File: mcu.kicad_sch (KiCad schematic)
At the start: 34 parts, among them J2 USB-C, J3 UART0, J4 I2C / Qwiic, J5 SPI, J6 WS2812, J7 Spare IO, J8 Rail break-out, SW1 RESET, SW2 BOOT, U4 ESP32-S3-WROOM-1-N16R8, U5 USBLC6-2SC6, U6 74AHCT1G125

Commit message: Power-fail ride-through: detect, coast, shed; board grows to 84 x 100
The ignition cuts this board's power with a log file open, every drive.
Three new pieces make that survivable, all simulated before layout:

- Detect: TLV431 + 100k/12.7k divider on VBAT_F, AHEAD of the ideal
  diode, asserting PWR_FAIL (IO15) at 11.0 V with ~0.3 V hysteresis.
  The harness collapses microseconds after the key turns while +VBAT
  coasts, so the warning costs no stored energy.
- Coast: two 220 uF/100 V cans join the 100 uF on +VBAT. 540 uF on the
  input rail, where a volt of headroom is worth most.
- Shed: AO3401 + 2N7002 high-side switch on the sensor rail (SENS_EN,
  IO16, off at reset), with PF1 moved behind it so a tripped sensor
  fuse can also be power-cycled from firmware.

Simulated end to end: detection <1 ms after the cut, then 108 ms to
converter dropout with sensors shed, 53 ms without -- the switch doubles
the flush budget. ISO pulse 1's brownout shortens from 8.2 to 5.6 ms.

The two cans plus the detector had no free board left on 84 x 84, so the
board grows to 84 x 100 (still JLC's cheap tier): bottom-edge furniture
and mounting holes move down 16 mm, one can per side, and the detector/
switch column gets its own placement zone. Also included from the audit:
the 3V3 buck's own input capacitor pair at its VIN pin (it was reaching
12.6 mm across to the 5 V island's), the CAN transceiver and AHCT buffer
bypasses pinned at their pins, and Power-class tracks at 0.55 mm to clear
IPC-2221 for 2 A at a 20 C rise.

Hard-won generator fix: a literal newline inside a symbol property is
accepted by KiCad's loader but silently breaks connectivity for every
symbol after it in the file -- the netlist dropped 45 components with no
error pointing anywhere near the cause. The emitter now flattens all
whitespace in property strings.

Board: 0 DRC violations, 0 unconnected, physical audit clean end to end.
185 components, 111 nets, ERC clean, netlist verified node-for-node.

Co-Authore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
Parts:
- removed C21: 1uF, Capacitor_SMD:C_0805_2012Metric, symbol Device:C
- removed C22, C25: 10uF, Capacitor_SMD:C_1206_3216Metric, symbol Device:C
- removed C23, C24: 100nF, Capacitor_SMD:C_0805_2012Metric, symbol Device:C
- removed R16, R17, R22: 10k, Resistor_SMD:R_0805_2012Metric, symbol Device:R
- removed R18, R19: 5.1k, Resistor_SMD:R_0805_2012Metric, symbol Device:R
- removed R20, R21: 4.7k, Resistor_SMD:R_0805_2012Metric, symbol Device:R
- removed U4: ESP32-S3-WROOM-1-N16R8, RF_Module:ESP32-S3-WROOM-1, symbol RF_Module:ESP32-S3-WROOM-1
- added C28, C29, C31, C32: 100nF, Capacitor_SMD:C_0805_2012Metric, symbol Device:C
- added C30: 10uF, Capacitor_SMD:C_1206_3216Metric, symbol Device:C
- added R28: 4.7k, Resistor_SMD:R_0805_2012Metric, symbol Device:R
- added R29, R32, R33, R34: 10k, Resistor_SMD:R_0805_2012Metric, symbol Device:R
- added R30: 33, Resistor_SMD:R_0805_2012Metric, symbol Device:R
- added R31: 100, Resistor_SMD:R_0805_2012Metric, symbol Device:R
- added U7: 74AHCT1G125, Package_TO_SOT_SMD:SOT-23-5, symbol 74xGxx:74AHCT1G125
- C26: value 100nF -> 1uF; Note USBLC6-2SC6 VBUS pin decoupling; the ST datasheet asks for 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 -> EN reset delay
- C27: value 100nF -> 10uF; footprint Capacitor_SMD:C_0805_2012Metric -> Capacitor_SMD:C_1206_3216Metric; Note AHCT decoupling -> (none)
- J7: Note IO3/IO45/IO46 are strapping pins, each with a 10k pull-down -- anything attached must not fight them at boot. IO15/IO16 are ordinary GPIOs, free since the status LEDs came off. The ground pin is here so a probe or a ribbon has a return -> IO3/IO45/IO46 are strapping pins, each with a 10k pull-down -- anything attached must not fight them at boot. Pins 4 and 5 are no longer spare: IO15 is the power-fail interrupt and IO16 is the sensor-rail enable. They stay on the header as probe points, so the ride-through can be watched on a scope without unsoldering anything, but nothing else may drive them. The ground pin is here so a probe or a ribbon has a return
- R23: value 33 -> 10k; Note Edge-rate limit into the level shifter -> (none)
- R24: value 100 -> 10k; Note Series termination into the strip. The buffer drove the con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 -> (none)
- R25: value 10k -> 5.1k; Note Strapping pin held low at boot -> (none)
- R26: value 10k -> 5.1k; Note Strapping pin: VDD_SPI = 3.3V -> (none)
- R27: value 10k -> 4.7k; Note Strapping pin: normal boot mode -> (none)
- U5: value USBLC6-2SC6 -> ESP32-S3-WROOM-1-N16R8; footprint Package_TO_SOT_SMD:SOT-23-6 -> RF_Module:ESP32-S3-WROOM-1; symbol Power_Protection:USBLC6-2SC6 -> RF_Module:ESP32-S3-WROOM-1; MPN USBLC6-2SC6 -> ESP32-S3-WROOM-1-N16R8; Note USB ESD clamp -> 16MB flash / 8MB octal PSRAM. Pins 28-30 (IO35/36/37) are c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
- U6: value 74AHCT1G125 -> USBLC6-2SC6; footprint Package_TO_SOT_SMD:SOT-23-5 -> Package_TO_SOT_SMD:SOT-23-6; symbol 74xGxx:74AHCT1G125 -> Power_Protection:USBLC6-2SC6; MPN SN74AHCT1G125DBVR -> USBLC6-2SC6; Note 5 V buffer so WS2812 DIN is a real 5 V rail, not 3.3 V hopi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 -> USB ESD clamp
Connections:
- net +3V3: now also C27.1, R23.1, R24.1, R27.1, U5.2 (3V3), C28.1, C29.1, R28.1, R29.2
- net +5V: now also C32.1, U7.5 (VCC); no longer C27.1, U6.5 (VCC)
- net AIN1: now also U5.39 (IO1)
- net AIN2: now also U5.38 (IO2)
- net AIN3: now also U5.4 (IO4)
- net AIN4: now also U5.5 (IO5)
- net CAN_RX: now also U5.11 (IO18)
- net CAN_S: now also U5.23 (IO21)
- net CAN_TX: now also U5.10 (IO17)
- net GND: now also U5.1 (GND), U5.40 (GND), U5.41 (GND), U6.2 (GND), C28.2, C29.2, C30.2, C31.2, C32.2, R32.2, R33.2, R34.2, U7.1, U7.3 (GND); no longer R27.2, U5.2 (GND), U6.1, U6.3 (GND)
- net I2C_SCL: now also U5.32 (IO39), R28.2
- net I2C_SDA: now also R27.2, U5.31 (IO38)
- net IO3: now also U5.15 (IO3), R32.1; no longer R25.1
- net IO45: now also U5.26 (IO45), R33.1; no longer R26.1
- net IO46: now also U5.16 (IO46), R34.1; no longer R27.1
- net LED_DIN: now also R31.1, U7.4; no longer R24.1, U6.4
- net LED_DIN_A: now also R30.2, U7.2; no longer R23.2, U6.2
- net LED_DIN_J: now also R31.2; no longer R24.2
- net LED_DIN_MCU: now also U5.25 (IO48), R30.1; no longer R23.1
- net MCU_BOOT: now also R24.2, U5.27 (IO0)
- net MCU_EN: now also C26.1, R23.2, U5.3 (EN)
- net SD_CD: now also U5.12 (IO8)
- net SD_CLK: now also U5.22 (IO14)
- net SD_CMD: now also U5.21 (IO13)
- net SD_D0: now also U5.20 (IO12)
- net SD_D1: now also U5.19 (IO11)
- net SD_D2: now also U5.18 (IO10)
- net SD_D3: now also U5.17 (IO9)
- net SD_PWR_EN: now also U5.7 (IO7)
- net SPI_CS: now also U5.24 (IO47), R29.1
- net SPI_MISO: now also U5.34 (IO41)
- net SPI_MOSI: now also U5.35 (IO42)
- net SPI_SCK: now also U5.33 (IO40)
- net UART_RX: now also U5.36 (RXD0)
- net UART_TX: now also U5.37 (TXD0)
- net USB_CC1: now also R25.1
- net USB_CC2: now also R26.1
- net USB_DM: now also U5.13 (USB_D-), U6.4 (I/O2); no longer U5.4 (I/O2)
- net USB_DM_CON: now also U6.3 (I/O2); no longer U5.3 (I/O2)
- net USB_DP: now also U5.14 (USB_D+), U6.6 (I/O1); no longer U5.6 (I/O1)
- net USB_DP_CON: now also U6.1 (I/O1); no longer U5.1 (I/O1)
- net VBAT_SNS: now also U5.6 (IO6)
- net VBUS: now also U6.5 (VBUS), C30.1, C31.1; no longer C26.1, U5.5 (VBUS)
- net IO15 renamed PWR_FAIL
- net PWR_FAIL: now also U5.8 (IO15)
- net IO16 renamed SENS_EN
- net SENS_EN: now also U5.9 (IO16)
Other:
- moved on the sheet: C26, C27, R23, R24, R25, R26, R27

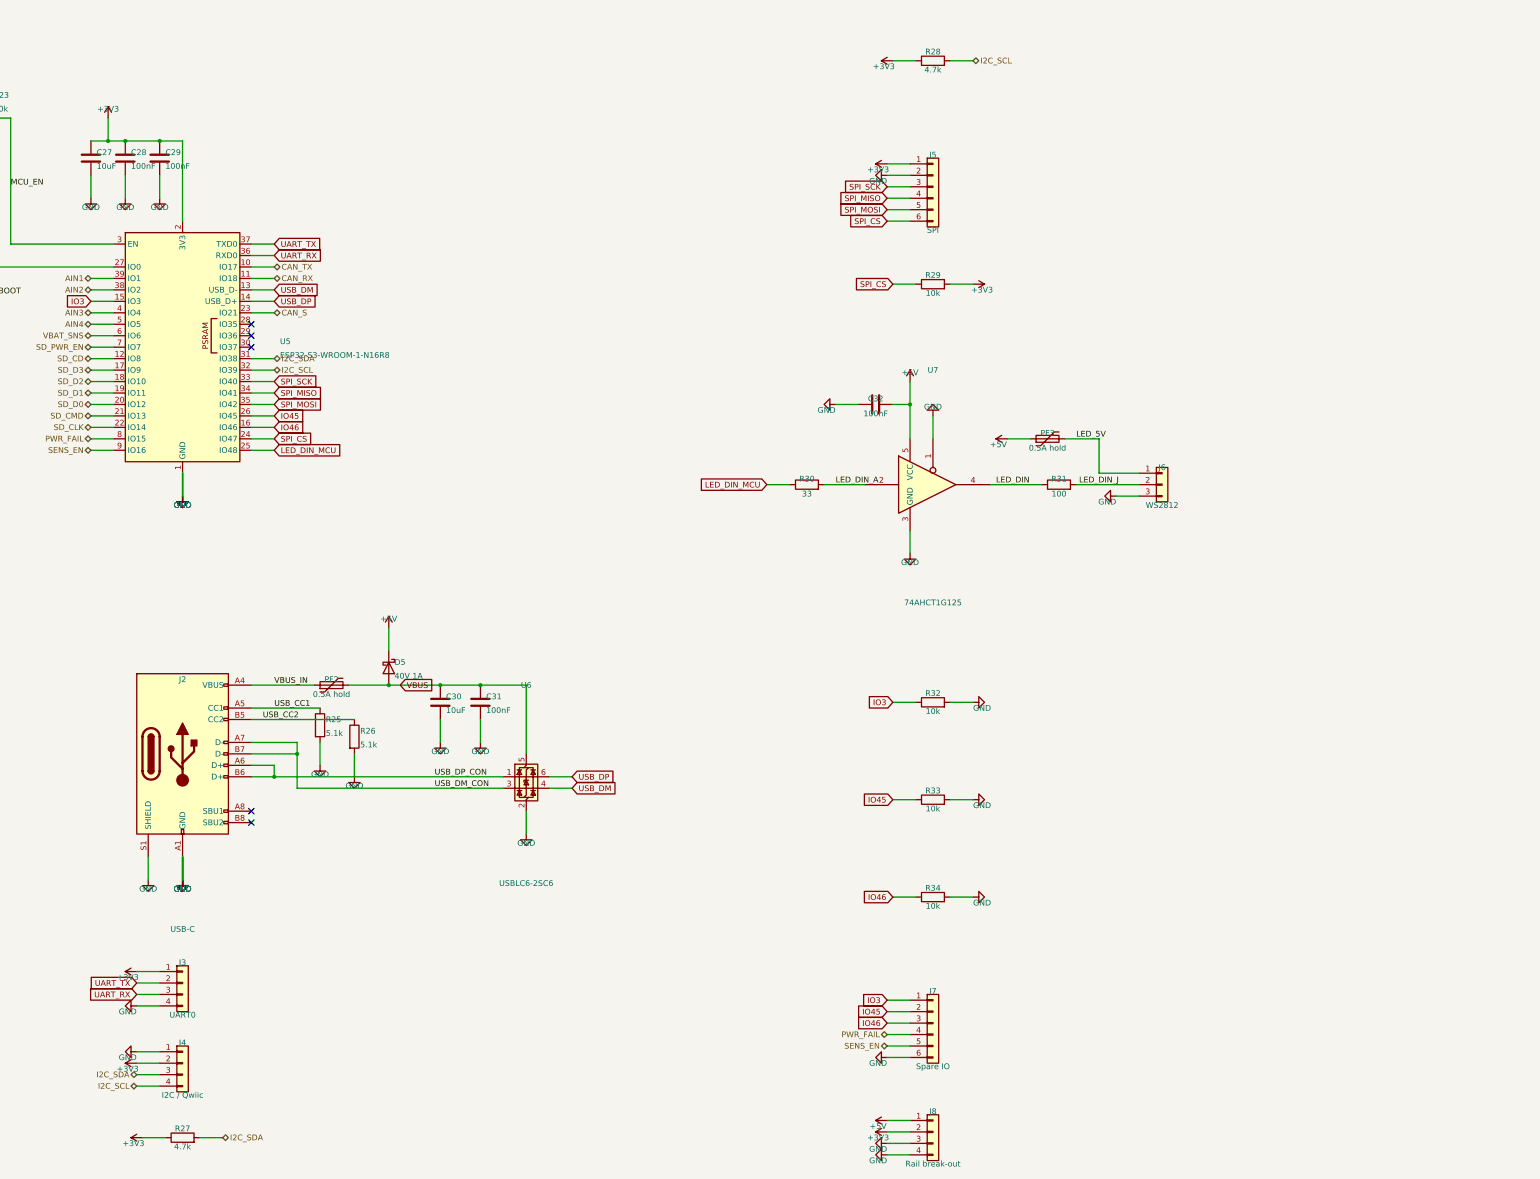
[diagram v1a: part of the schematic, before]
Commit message: USB OVP, card-slot ESD, SD test points, and a gold-standard schematic
Hardware, all simulation- or review-driven:
- USB overvoltage cutoff: TLV431 + AO3401 + MMBT3906 series switch on
  VBUS, tripping at 5.77 V. Re-simulated: a compliant 5 V source passes
  at 4.99 V, the switch opens at 5.95 V of brick, and the +5V rail never
  exceeds 5.2 V from anything up to 14 V -- where a 9 V brick previously
  drove it to 8.4 V against the TJA1051's 6 V absolute maximum.
  Off-the-shelf OVP parts were rejected first: the TPS25200 class cuts
  off near 7 V, which is no protection for a 6 V limit.
- Two SRV05-4 arrays clamp every microSD card contact (LCSC C13612);
  until now the ESP32's ~2 kV pin diodes were all that stood behind a
  card swapped by hand after every session.
- A second USBLC6 clamps the USB-C CC pins -- the first contacts every
  plug insertion touches, previously landing on bare 5.1k resistors.
- Test points on SD_CLK and SD_CMD, the most likely scope targets at
  bring-up and otherwise reachable only on fine-pitch pads.

The schematic itself was rebuilt to read like a reference design
(RejsaCAN was the benchmark): every circuit is now a hand-drawn block --
power-fail detector, sensor-rail switch, USB OVP, connector pull-
resistor clusters, and a single utility panel for test points, ERC
flags, mounting holes and the power LED. Sentence-length values became
part numbers ("0.2A PTC", "AO3401A", "600R") with ratings kept in
hidden fields, which also answers the external review's value-hygiene
findings. Title blocks carry rev B and a date. The Power sheet shrank
from A2 back to A3 in the process.

gen/README.md now documents the whole pipeline -- stages, the block-
drawing conventions with per-rotation pin geometry, the junction rules,
and the traps (property newlines, off-grid points, anchors keeping
their natural rotation) -- so the next board reuses all of it.

Board: 84 x 100, 0 DRC violations, 0 unconnected, 0 courtyard overlaps,
physical audit clean. BOM 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
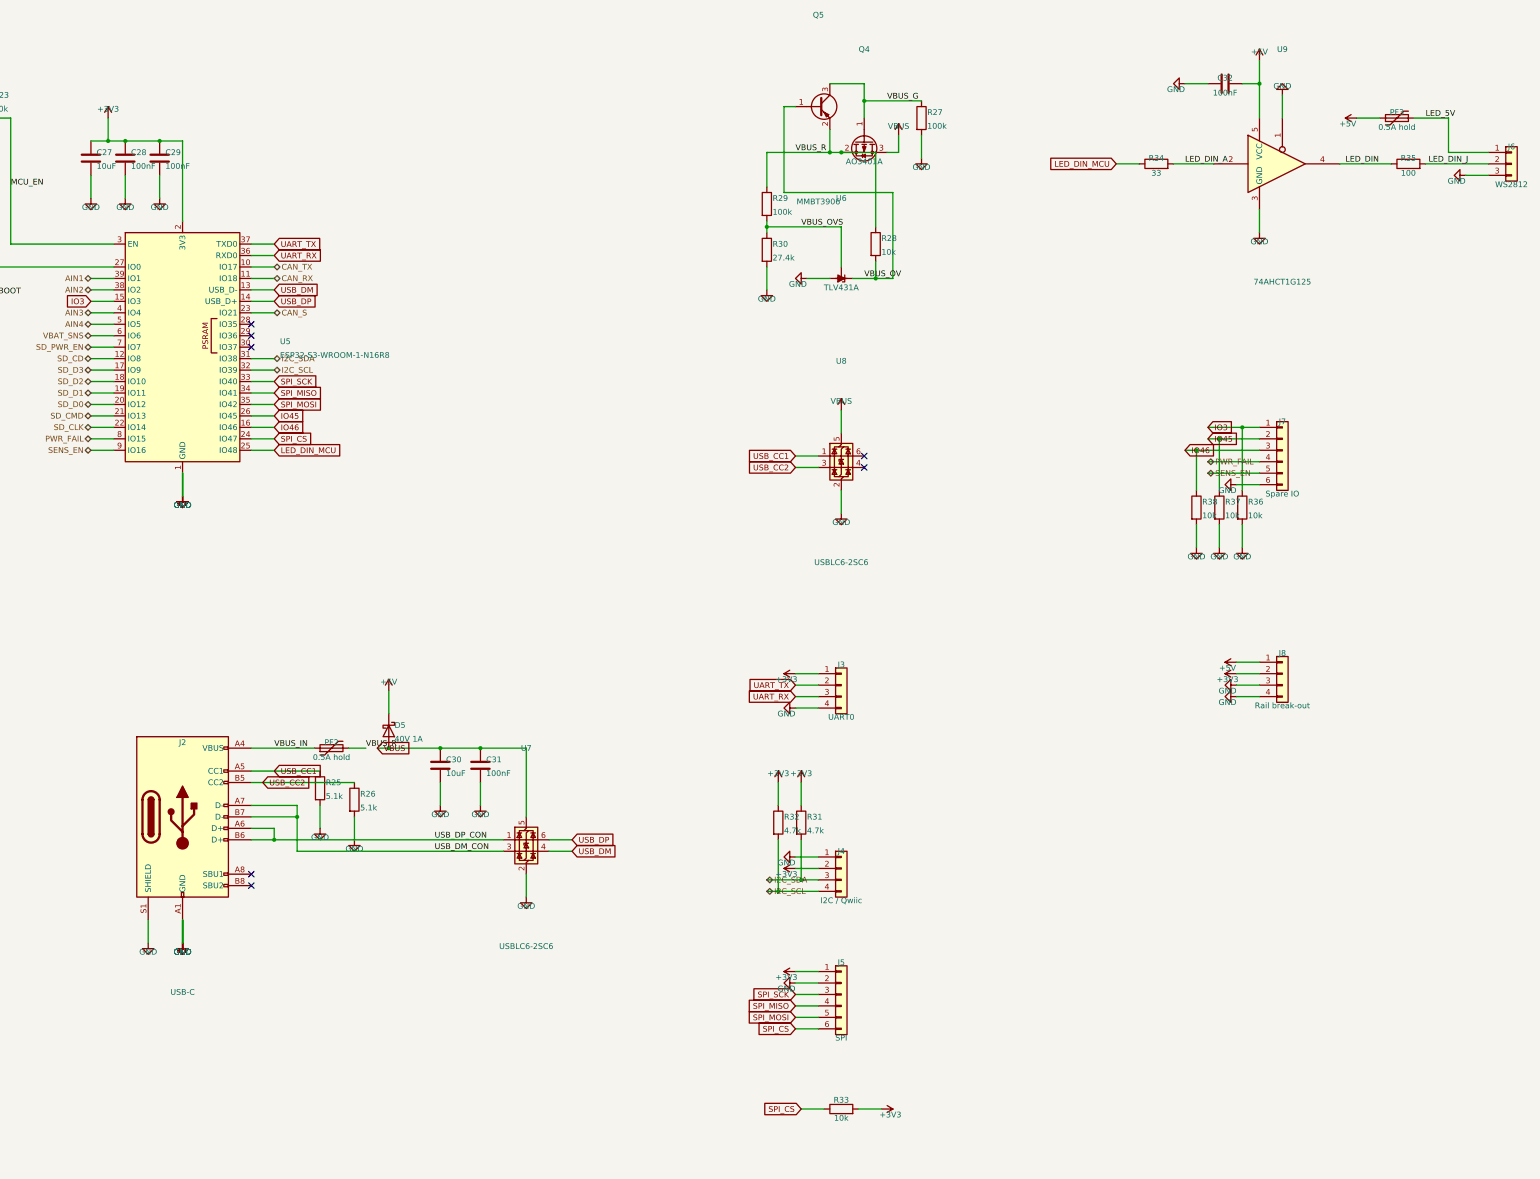
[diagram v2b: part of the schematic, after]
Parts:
- added Q4: AO3401A, Package_TO_SOT_SMD:SOT-23, symbol Transistor_FET:Q_PMOS_GSD
- added Q5: MMBT3906, Package_TO_SOT_SMD:SOT-23, symbol Transistor_BJT:Q_PNP_BEC
- added R35: 100, Resistor_SMD:R_0805_2012Metric, symbol Device:R
- added R36, R37, R38: 10k, Resistor_SMD:R_0805_2012Metric, symbol Device:R
- added U8: USBLC6-2SC6, Package_TO_SOT_SMD:SOT-23-6, symbol Power_Protection:USBLC6-2SC6
- added U9: 74AHCT1G125, Package_TO_SOT_SMD:SOT-23-5, symbol 74xGxx:74AHCT1G125
- R27: value 4.7k -> 100k; Note (none) -> Switch on by default
- R28: value 4.7k -> 10k; Note (none) -> Holds the PNP off while the TLV431 is not conducting
- R29: value 10k -> 100k; Note Holds an attached slave deselected until firmware drives IO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 -> OVP divider upper leg; Tolerance (none) -> 1%
- R30: value 33 -> 27.4k; Note Edge-rate limit into the level shifter -> Trip at 1.24V x 127.4/27.4 = 5.77V: above a compliant sourc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; Tolerance (none) -> 1%
- R31: value 100 -> 4.7k; Note Series termination into the strip. The buffer drove the con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 -> (none)
- R32: value 10k -> 4.7k; Note Strapping pin held low at boot -> (none)
- R33: Note Strapping pin: VDD_SPI = 3.3V -> Holds an attached slave deselected until firmware drives IO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
- R34: value 10k -> 33; Note Strapping pin: normal boot mode -> Edge-rate limit into the level shifter
- U6: value USBLC6-2SC6 -> TLV431A; footprint Package_TO_SOT_SMD:SOT-23-6 -> Package_TO_SOT_SMD:SOT-23; symbol Power_Protection:USBLC6-2SC6 -> Reference_Voltage:TL431DBZ; MPN USBLC6-2SC6 -> TLV431ASN1T1G; Note USB ESD clamp -> OVP comparator; conducts above the divider trip and opens t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
- U7: value 74AHCT1G125 -> USBLC6-2SC6; footprint Package_TO_SOT_SMD:SOT-23-5 -> Package_TO_SOT_SMD:SOT-23-6; symbol 74xGxx:74AHCT1G125 -> Power_Protection:USBLC6-2SC6; MPN SN74AHCT1G125DBVR -> USBLC6-2SC6; Note 5 V buffer so WS2812 DIN is a real 5 V rail, not 3.3 V hopi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 -> USB ESD clamp, behind the OVP switch so its own 5.5 V VBUS-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
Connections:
- net +3V3: now also R31.1, R32.1, R33.2; no longer R27.1, R28.1, R29.2
- net +5V: now also U9.5 (VCC); no longer U7.5 (VCC)
- net GND: now also R27.2, R30.2, U6.3 (A), U7.2 (GND), R36.2, R37.2, R38.2, U8.2 (GND), U9.1, U9.3 (GND); no longer R32.2, R33.2, R34.2, U6.2 (GND), U7.1, U7.3 (GND)
- net I2C_SCL: now also R32.2; no longer R28.2
- net I2C_SDA: now also R31.2; no longer R27.2
- net IO3: now also R36.1; no longer R32.1
- net IO45: now also R37.1; no longer R33.1
- net IO46: now also R38.1; no longer R34.1
- net LED_DIN: now also R35.1, U9.4; no longer R31.1, U7.4
- net LED_DIN_A: now also R34.2, U9.2; no longer R30.2, U7.2
- net LED_DIN_J: now also R35.2; no longer R31.2
- net LED_DIN_MCU: now also R34.1; no longer R30.1
- net SPI_CS: now also R33.1; no longer R29.1
- net USB_CC1: now also U8.1 (I/O1)
- net USB_CC2: now also U8.3 (I/O2)
- net USB_DM: now also U7.4 (I/O2); no longer U6.4 (I/O2)
- net USB_DM_CON: now also U7.3 (I/O2); no longer U6.3 (I/O2)
- net USB_DP: now also U7.6 (I/O1); no longer U6.6 (I/O1)
- net USB_DP_CON: now also U7.1 (I/O1); no longer U6.1 (I/O1)
- net VBUS: now also U7.5 (VBUS), Q4.3 (D), U8.5 (VBUS); no longer PF2.2, U6.5 (VBUS)
- new net VBUS_G: Q4.1 (G), Q5.3 (C), R27.1
- new net VBUS_OV: Q5.1 (B), R28.2, U6.1 (K)
- new net VBUS_OVS: R29.2, R30.1, U6.2 (REF)
- new net VBUS_R: PF2.2, Q4.2 (S), Q5.2 (E), R28.1, R29.1
- no-connect marks 5 -> 7
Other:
- moved on the sheet: C30, C31, C32, D5, J2, J3, J4, J5, J6, J7, J8, PF2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
